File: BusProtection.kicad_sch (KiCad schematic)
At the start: 102 parts, among them Q1 MMBT2907, Q10 BSS138DWQ-7, Q11 BSS138DWQ-7, Q12 MBT2222ADW1T1, Q13 MBT2222ADW1T1, Q14 BSS138DWQ-7, Q15 BSS138DWQ-7, Q16 MBT2222ADW1T1, Q17 MBT2222ADW1T1, Q18 MMBT2907, Q2 BSS138DWQ-7, Q20 BSS138DWQ-7, Q21 MBT2222ADW1T1, Q22 BSS138DWQ-7, Q23 MBT2222ADW1T1, Q3 BSS138DWQ-7, Q4 MBT2222ADW1T1, Q5 MBT2222ADW1T1, Q6 BSS138DWQ-7, Q7 BSS138DWQ-7, Q8 MBT2222ADW1T1, Q9 MBT2222ADW1T1

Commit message: Some fixes
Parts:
- renumbered Q22 to Q19, Q23 to Q22, R107 to R2
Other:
- note removed: "Bus Protection"
- moved on the sheet: C36, C37, Q1, Q19A, Q19B, Q20A, Q20B, Q21A, Q21B, Q22A, Q22B, R100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

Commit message: Finished B2/01 Updates
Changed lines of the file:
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@@
   (title_block
     (title "PyCubed Mini")
-    (date "2022-09-06")
-    (rev "B1/04")
+    (date "2022-10-09")
+    (rev "B2/01")
     (company "RExLab Carnegie Mellon University")
     (comment 1 "Z. Manchester")
@@
   )
   (text "mainboard" (at 350.393 245.872 0)
-    (effects (font (size 3.9878 3.9878) (thickness 0.7976) bold) (justify left bottom))
+    (effects (font (size 3.81 3.81) (thickness 0.7976) bold) (justify left bottom))
   )
   (text "SPI Bus Protection - Radio" (at 286.258 35.052 0)

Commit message: Cleanup
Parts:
- Q1: renamed from Q2; value BSS138DWQ-7 -> NX3008NBKS; symbol mainboard:BSS138DWQ-7 -> mainboard:NX3008NBKS; Flight BSS138DWQ-7 -> (none); Manufacturer_Name Diodes Incorporated -> Nexperia USA Inc.; Manufacturer_Part_Number BSS138DWQ-7 -> NX3008NBKS
- Q11: renamed from Q14; value BSS138DWQ-7 -> NX3008NBKS; symbol mainboard:BSS138DWQ-7 -> mainboard:NX3008NBKS; Flight BSS138DWQ-7 -> (none); Manufacturer_Name Diodes Incorporated -> Nexperia USA Inc.; Manufacturer_Part_Number BSS138DWQ-7 -> NX3008NBKS
- Q13: renamed from Q11; value BSS138DWQ-7 -> NX3008NBKS; symbol mainboard:BSS138DWQ-7 -> mainboard:NX3008NBKS; Flight BSS138DWQ-7 -> (none); Manufacturer_Name Diodes Incorporated -> Nexperia USA Inc.; Manufacturer_Part_Number BSS138DWQ-7 -> NX3008NBKS
- Q15, Q19, Q7: value BSS138DWQ-7 -> NX3008NBKS; symbol mainboard:BSS138DWQ-7 -> mainboard:NX3008NBKS; Flight BSS138DWQ-7 -> (none); Manufacturer_Name Diodes Incorporated -> Nexperia USA Inc.; Manufacturer_Part_Number BSS138DWQ-7 -> NX3008NBKS
- Q17: renamed from Q20; value BSS138DWQ-7 -> NX3008NBKS; symbol mainboard:BSS138DWQ-7 -> mainboard:NX3008NBKS; Flight BSS138DWQ-7 -> (none); Manufacturer_Name Diodes Incorporated -> Nexperia USA Inc.; Manufacturer_Part_Number BSS138DWQ-7 -> NX3008NBKS
- Q3: renamed from Q6; value BSS138DWQ-7 -> NX3008NBKS; symbol mainboard:BSS138DWQ-7 -> mainboard:NX3008NBKS; Flight BSS138DWQ-7 -> (none); Manufacturer_Name Diodes Incorporated -> Nexperia USA Inc.; Manufacturer_Part_Number BSS138DWQ-7 -> NX3008NBKS
- Q5: renamed from Q3; value BSS138DWQ-7 -> NX3008NBKS; symbol mainboard:BSS138DWQ-7 -> mainboard:NX3008NBKS; Flight BSS138DWQ-7 -> (none); Manufacturer_Name Diodes Incorporated -> Nexperia USA Inc.; Manufacturer_Part_Number BSS138DWQ-7 -> NX3008NBKS
- Q9: renamed from Q10; value BSS138DWQ-7 -> NX3008NBKS; symbol mainboard:BSS138DWQ-7 -> mainboard:NX3008NBKS; Flight BSS138DWQ-7 -> (none); Manufacturer_Name Diodes Incorporated -> Nexperia USA Inc.; Manufacturer_Part_Number BSS138DWQ-7 -> NX3008NBKS
- R33: renamed from R53; value 0 -> DNI (0R)
- R34: renamed from R54; value 0 -> DNI (0R)
- R45: renamed from R55; value 0 -> DNI (0R)
- R46: renamed from R56; value 0 -> DNI (0R)
- R57, R58: value 0 -> DNI (0R)
- R69: renamed from R59; value 0 -> DNI (0R)
- R70: renamed from R60; value 0 -> DNI (0R)
- R81: renamed from R101; value 0 -> DNI (0R)
- R82: renamed from R102; value 0 -> DNI (0R)
- R93: renamed from R71; value 0 -> DNI (0R)
- R94: renamed from R91; value 0 -> DNI (0R)
- R95: renamed from R84; value 4.7k -> 4.7K
- R99: renamed from R90; value 4.7k -> 4.7K
- renumbered C24 to C28, C26 to C29, C25 to C30, C27 to C31, C28 to C32, C30 to C33, C29 to C34, C31 to C35, Q12 to Q10, Q16 to Q12, Q13 to Q14, Q17 to Q16, Q21 to Q18, Q4 to Q2, Q22 to Q20, Q18 to Q21, Q1 to Q22, Q8 to Q4, Q5 to Q6, Q9 to Q8, R83 to R100, R94 to R101, R95 to R102, R29 to R35, R31 to R36, R33 to R37, R35 to R38, R36 to R39, R39 to R40, R43 to R42, R45 to R43, R46 to R44, R30 to R47, R32 to R48, R34 to R49, R37 to R50, R38 to R51, R40 to R52, R42 to R53, R44 to R54, R47 to R55, R48 to R56, R49 to R59, R51 to R60, R63 to R62, R64 to R63, R67 to R64, R72 to R65, R74 to R66, R76 to R67, R77 to R68, R50 to R71, R52 to R72, R62 to R73, R65 to R74, R66 to R75, R68 to R76, R73 to R77, R75 to R78, R78 to R79, R79 to R80, R96 to R83, R97 to R84, R98 to R85, R99 to R86, R100 to R87, R103 to R88, R104 to R89, R105 to R90, R106 to R91, R2 to R92, R81 to R96, R86 to R97, R87 to R98
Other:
- note added: "IMU Jumper"
- note added: "Motor 1 Jumper"
- note added: "Motor 2 Jumper"
- note added: "Motor 3 Jumper"
- note added: "RTC Jumper"
- note added: "Radio Jumper"
- note added: "SD Card Jumper"
- moved on the sheet: C28, C29, C30, C31, C32, C33, C34, C35, C36, C37, Q10A, Q10B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

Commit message: Stash before major changes
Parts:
- R100, R96: value 0 -> 0R
- R35, R40, R47, R52, R59, R64, R71, R76, R83, R88: value 680 -> 680R

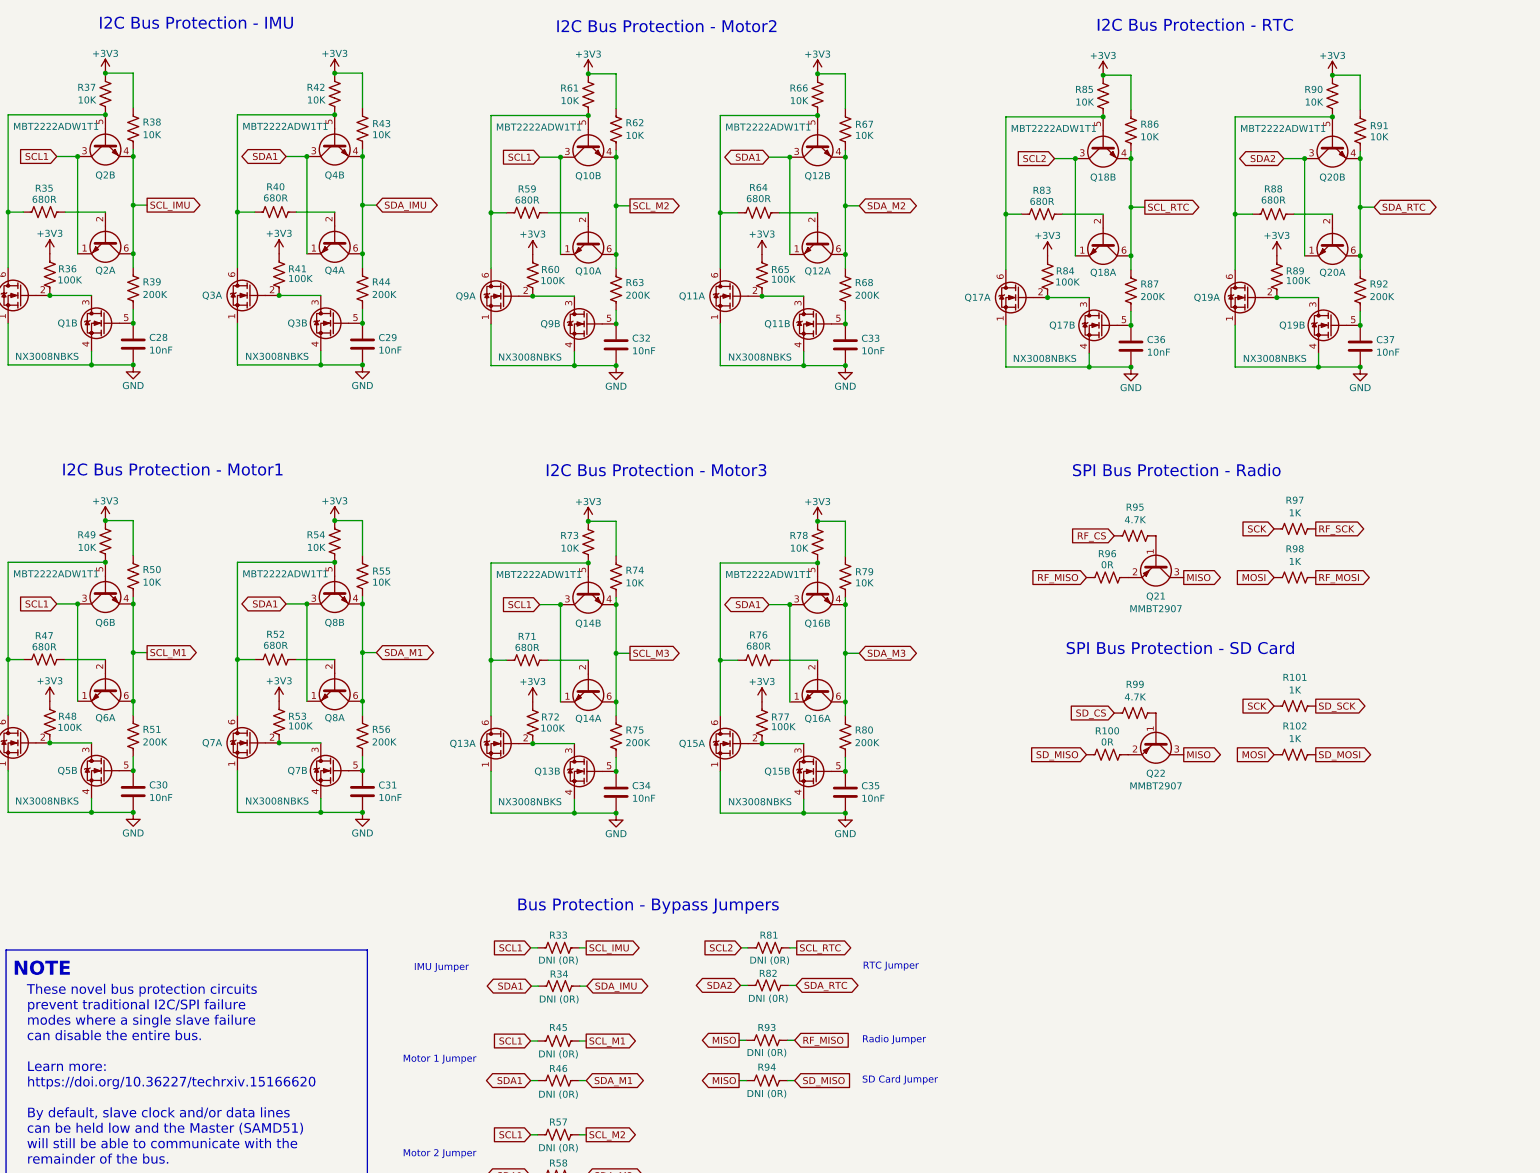
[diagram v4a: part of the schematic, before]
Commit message: Finished routing Rev B3/01
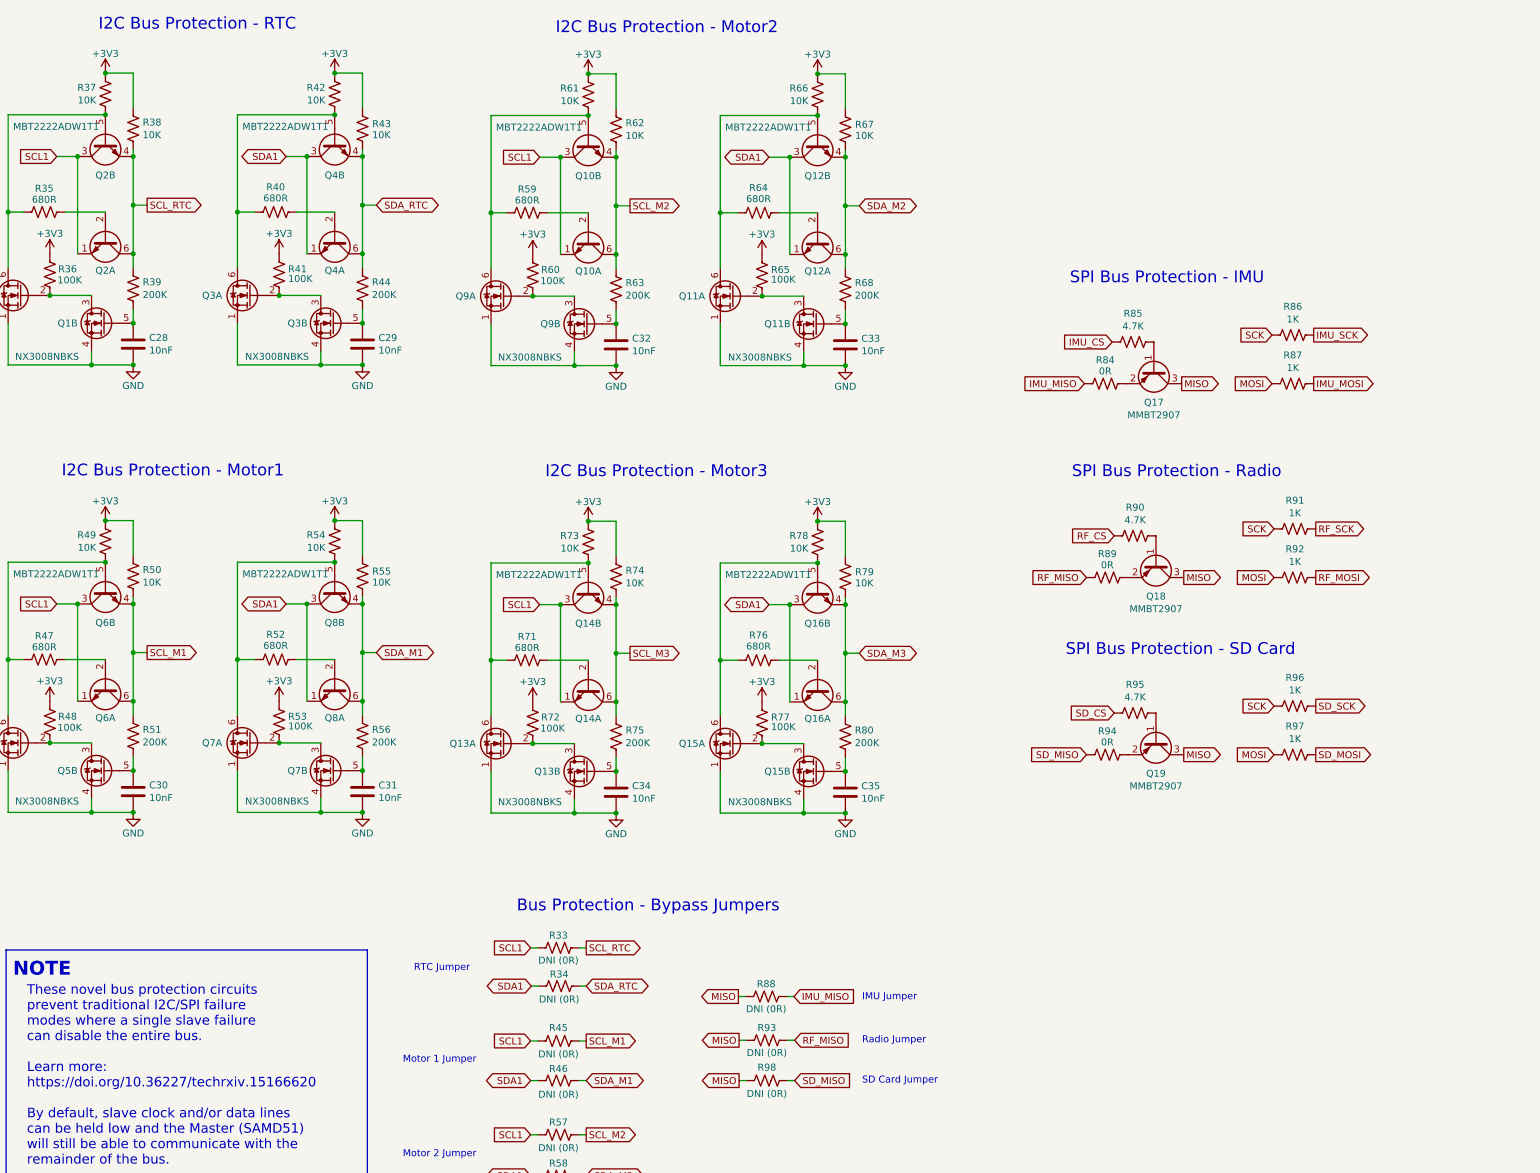
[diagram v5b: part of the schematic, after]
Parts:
- removed C36, C37: 10nF, Capacitor_SMD:C_0603_1608Metric, symbol Device:C
- removed Q17, Q19: NX3008NBKS, Package_TO_SOT_SMD:SOT-363_SC-70-6, symbol mainboard:NX3008NBKS
- removed Q18, Q20: MBT2222ADW1T1, Package_TO_SOT_SMD:SOT-363_SC-70-6, symbol Transistor_BJT:MBT2222ADW1T1
- removed R81, R82: DNI (0R), Resistor_SMD:R_0603_1608Metric, symbol Device:R_US
- removed R83: 680R, Resistor_SMD:R_0603_1608Metric, symbol Device:R_US
- removed R89: 100K, Resistor_SMD:R_0603_1608Metric, symbol Device:R_US
- removed R90, R91: 10K, Resistor_SMD:R_0603_1608Metric, symbol Device:R_US
- removed R92: 200K, Resistor_SMD:R_0603_1608Metric, symbol Device:R_US
- added Q17: MMBT2907, Package_TO_SOT_SMD:SOT-23, symbol mainboard:MMBT2907
- R84: value 100K -> 0R
- R85: value 10K -> 4.7K
- R86: value 10K -> 1K
- R87: value 200K -> 1K
- R88: value 680R -> DNI (0R); DNI (none) -> DNI
- renumbered Q21 to Q18, Q22 to Q19, R96 to R89, R95 to R90, R97 to R91, R98 to R92, R100 to R94, R99 to R95, R101 to R96, R102 to R97, R94 to R98
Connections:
- net SCL_IMU is gone; now on net SCL_RTC: Q2.4 (E2), Q2.6 (C1), R33.1, R38.2, R39.1
- net SDA_IMU is gone; now on net SDA_RTC: Q4.4 (E2), Q4.6 (C1), R34.1, R43.2, R44.1
- net +3V3: no longer R84.1, R85.1, R86.1
- net MISO: now also R88.2, Q17.3 (C)
- net MOSI: now also R87.2
- net SCK: now also R86.2
- net SCL_RTC: no longer R86.2, R87.1
- net IMU_MISO: now reaches R84.2
- net IMU_MISO: now also R88.1
- net IMU_CS: now reaches R85.2
- new net: Q17.2 (E), R84.1
- new net: Q17.1 (B), R85.1
- new net IMU_MOSI: R87.1
- new net IMU_SCK: R86.1
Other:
- note added: "SPI Bus Protection - IMU"
- note removed: "I2C Bus Protection - IMU"

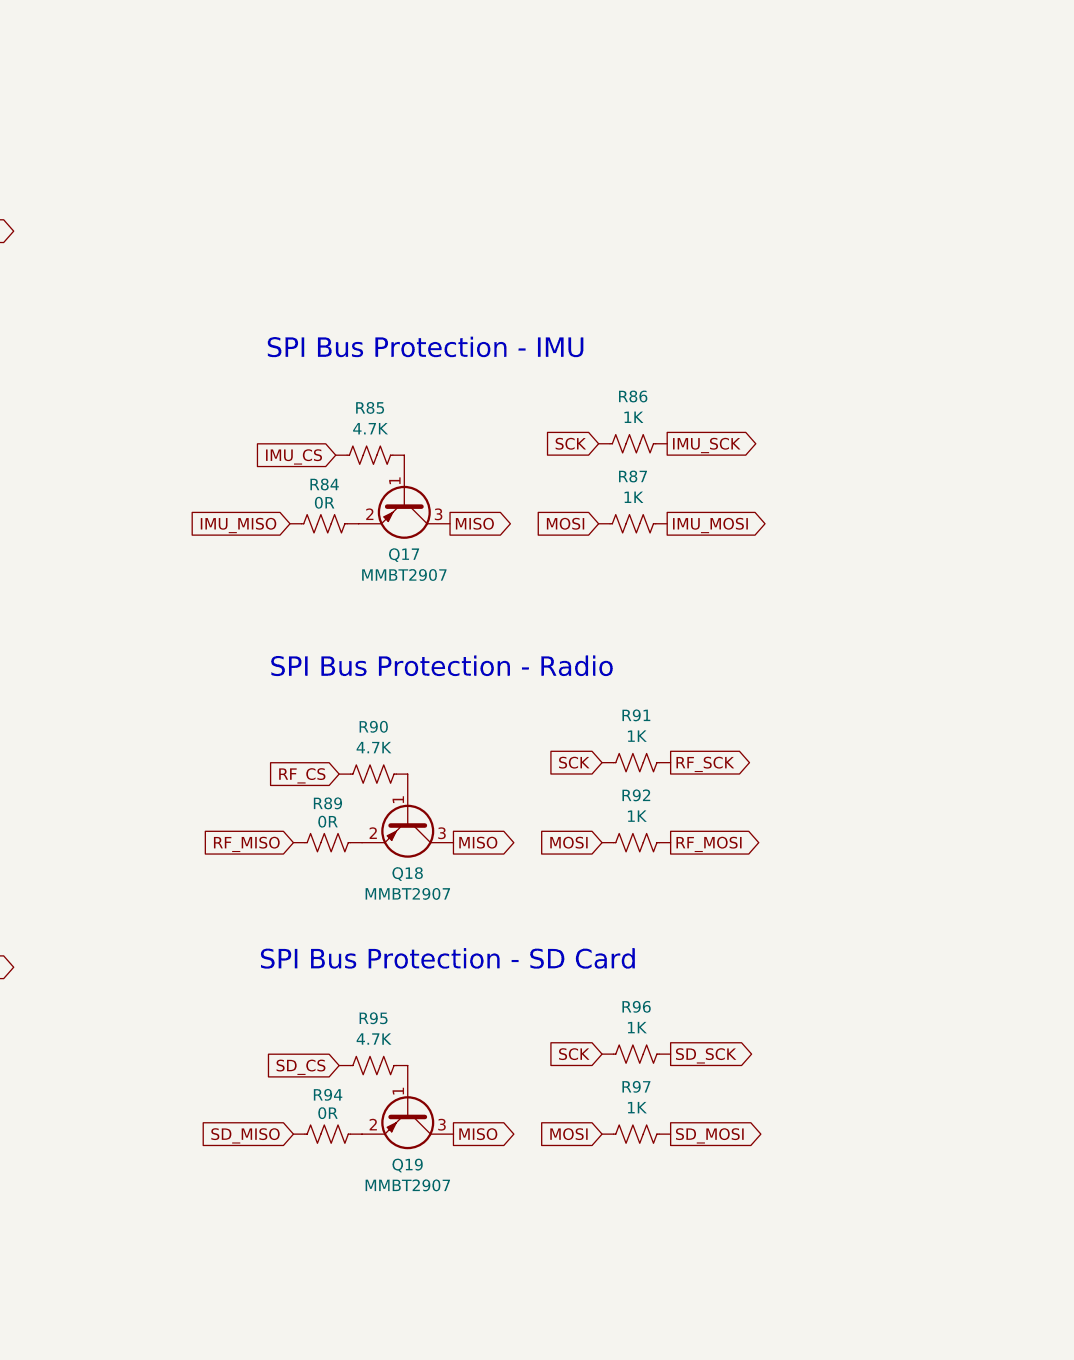
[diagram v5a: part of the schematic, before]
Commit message: Updated Schematic to reflect RTC on I2C 1
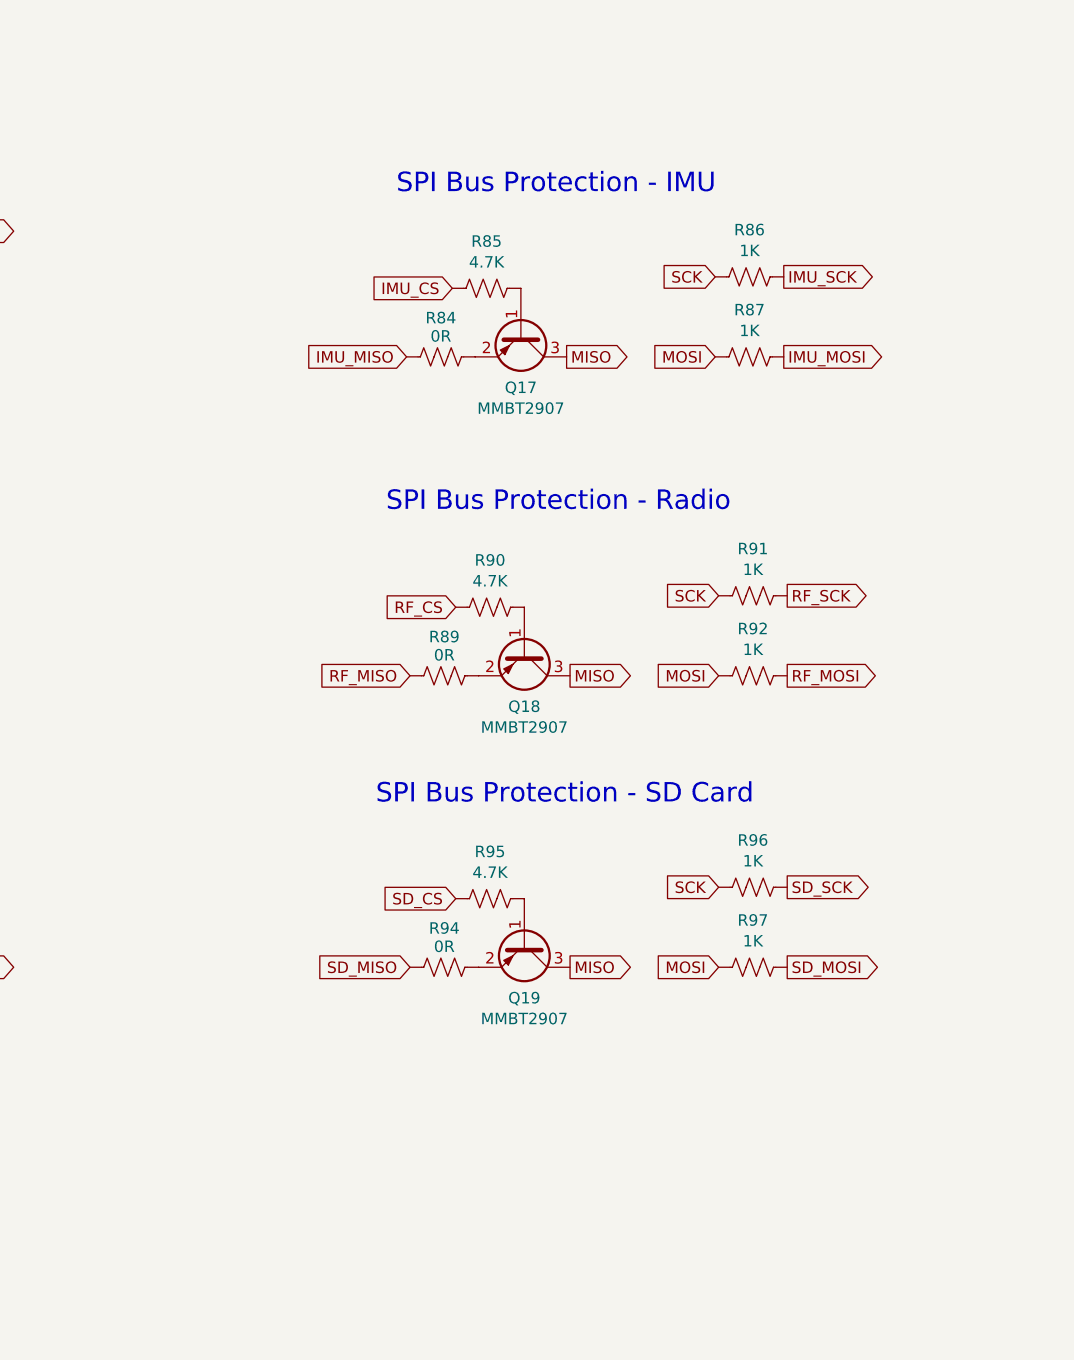
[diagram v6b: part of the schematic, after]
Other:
- moved on the sheet: Q17, Q18, Q19, R84, R85, R86, R87, R89, R90, R91, R92, R94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
